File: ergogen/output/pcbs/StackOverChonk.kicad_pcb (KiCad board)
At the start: 2 copper layers, 138.9 x 113.2 mm, 93 parts

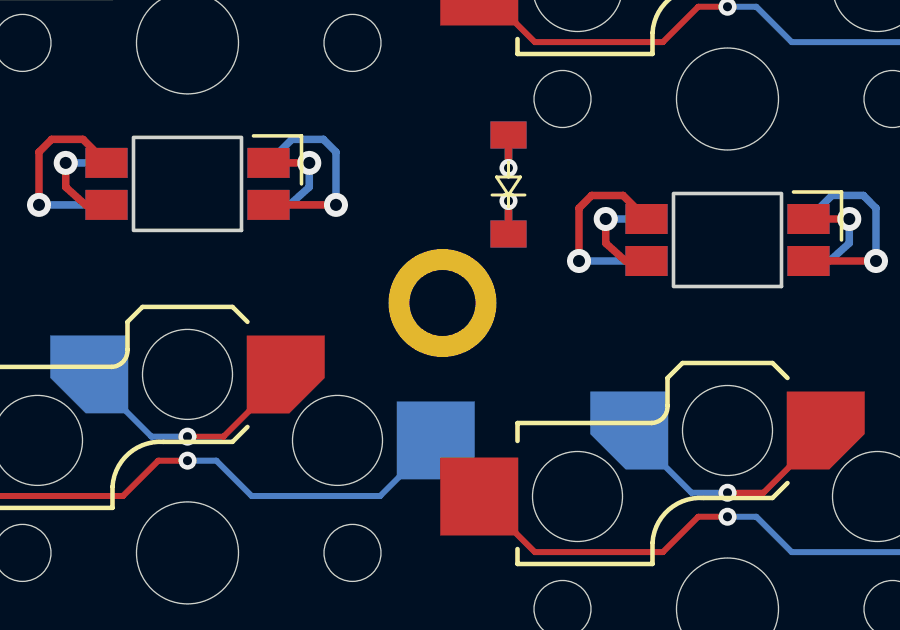
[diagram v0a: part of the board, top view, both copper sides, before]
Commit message: hole fixes
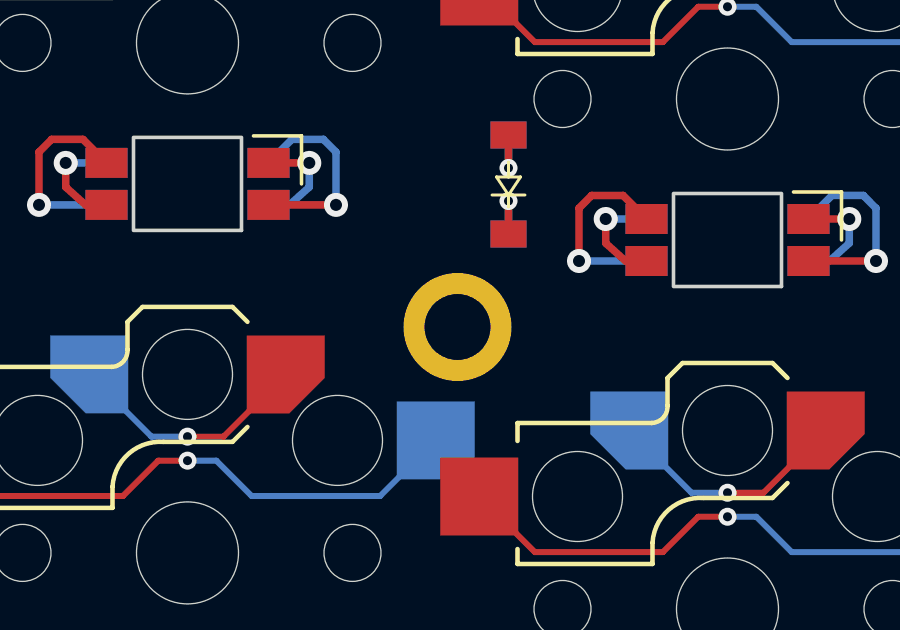
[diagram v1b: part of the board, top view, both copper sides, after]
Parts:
- moved H4 0.94 mm to (181.0, 84.0)
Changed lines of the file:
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@@
   (footprint "ceoloide:mounting_hole_plated"
     (layer "B.Cu")
-    (at 180.5 83.17 0)
+    (at 181 83.97 0)
     (property "Reference" "H4"
       (at 0 3 0)

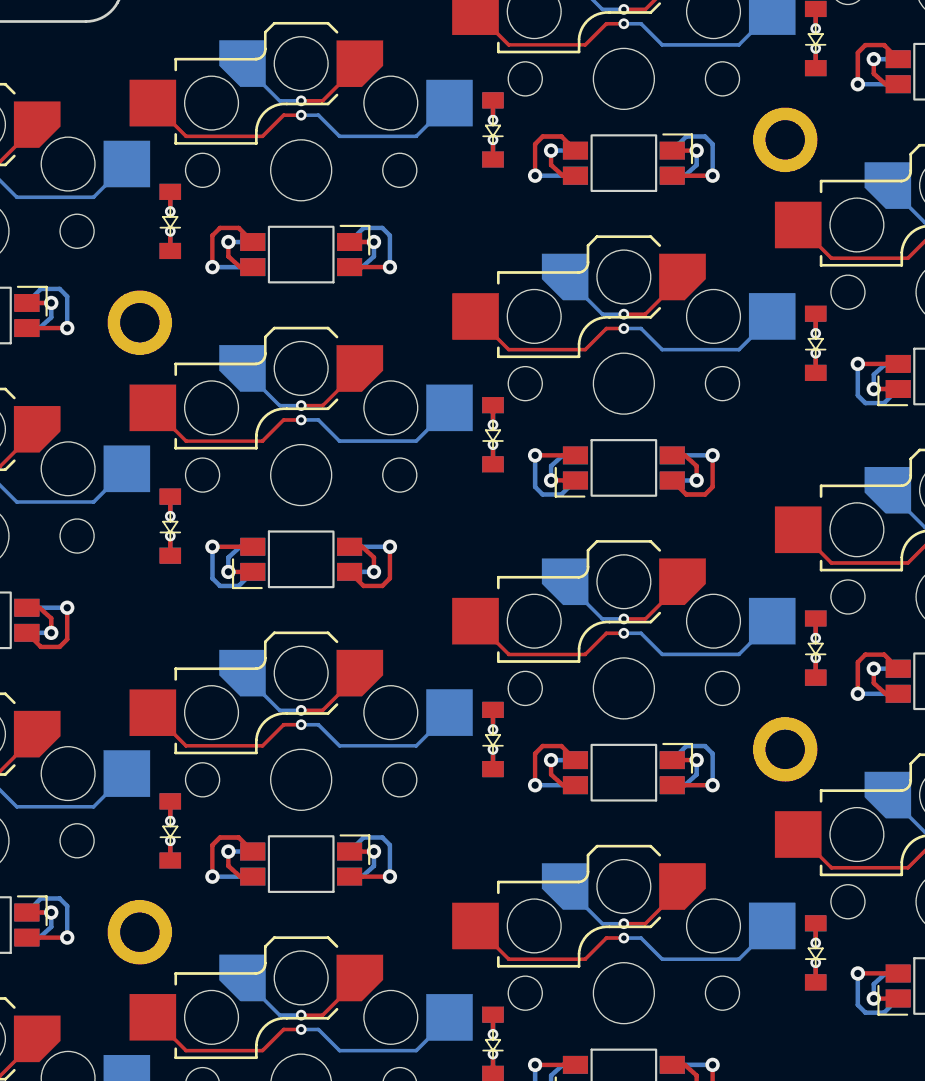
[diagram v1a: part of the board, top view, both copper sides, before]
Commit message: hole fixes
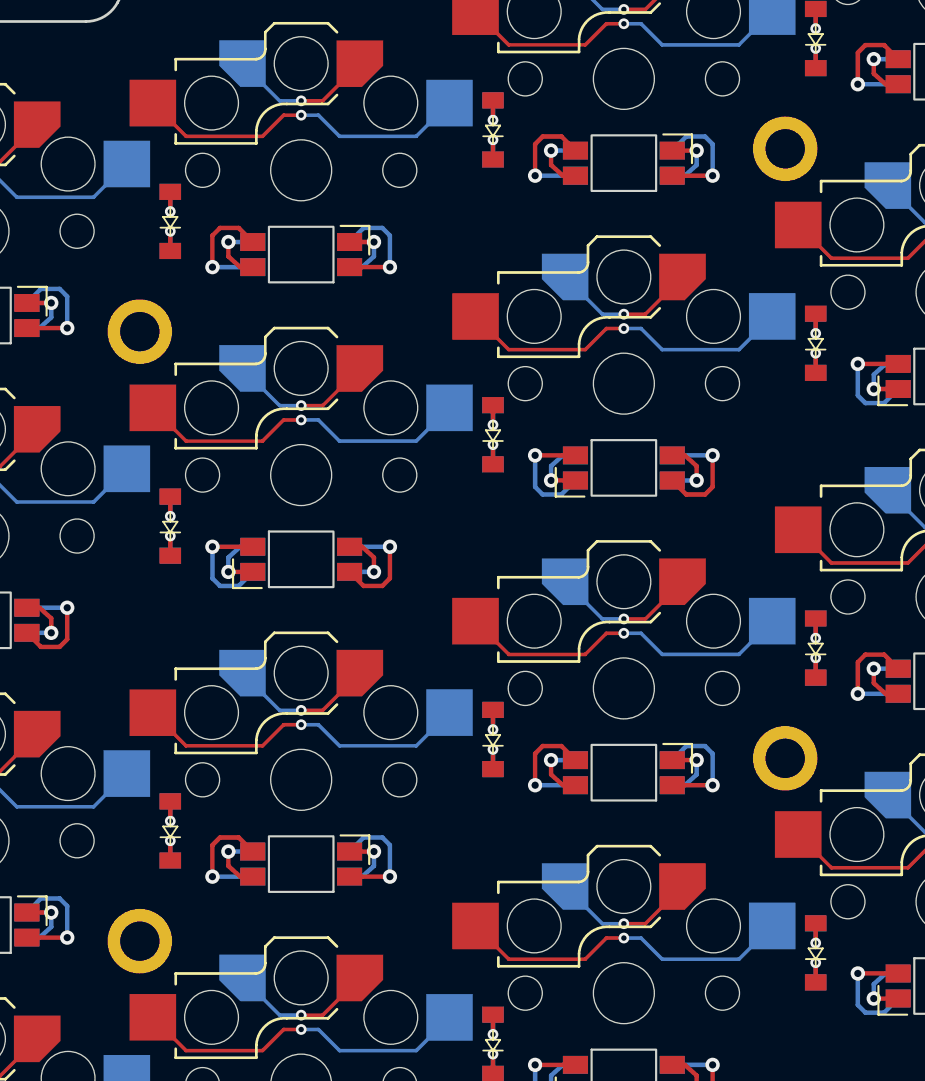
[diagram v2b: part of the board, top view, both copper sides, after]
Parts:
- moved H1 0.50 mm to (109.0, 54.6)
- moved H2 0.50 mm to (109.0, 88.6)
- moved H5 0.50 mm to (145.0, 78.4)
- moved H6 0.50 mm to (145.0, 44.4)
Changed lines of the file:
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@@
   (footprint "ceoloide:mounting_hole_plated"
     (layer "B.Cu")
-    (at 109 54.099999999999994 0)
+    (at 109 54.599999999999994 0)
     (property "Reference" "H1"
       (at 0 3 0)
@@
   (footprint "ceoloide:mounting_hole_plated"
     (layer "B.Cu")
-    (at 109 88.1 0)
+    (at 109 88.6 0)
     (property "Reference" "H2"
       (at 0 3 0)
@@
   (footprint "ceoloide:mounting_hole_plated"
     (layer "B.Cu")
-    (at 145 77.9 0)
+    (at 145 78.4 0)
     (property "Reference" "H5"
       (at 0 3 0)
@@
   (footprint "ceoloide:mounting_hole_plated"
     (layer "B.Cu")
-    (at 145 43.900000000000006 0)
+    (at 145 44.400000000000006 0)
     (property "Reference" "H6"
       (at 0 3 0)
